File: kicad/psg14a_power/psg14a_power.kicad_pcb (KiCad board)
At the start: 2 copper layers, 9 parts, among them Q1 IRF9Z24N

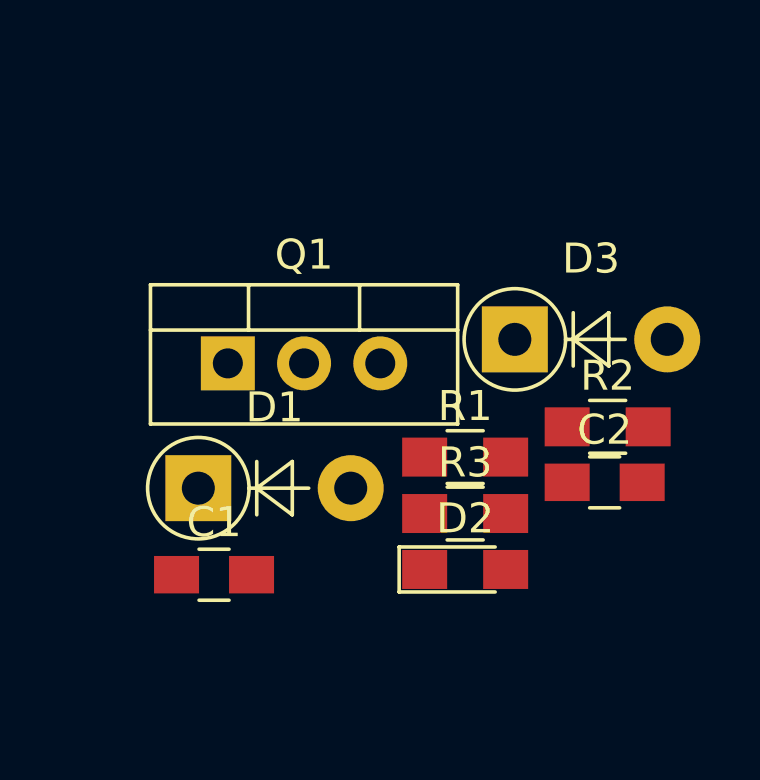
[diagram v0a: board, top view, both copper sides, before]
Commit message: [psg14a-power]Components placed
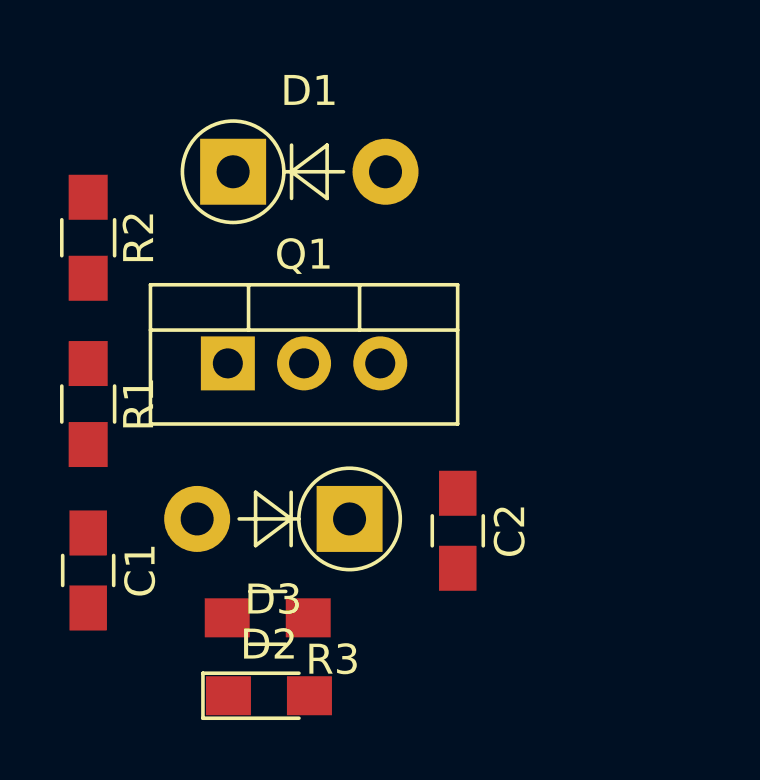
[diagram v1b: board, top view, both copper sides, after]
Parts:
- moved R2 18.4 mm to (44.2, 35.4), turned to 270 degrees
- moved R1 12.7 mm to (44.2, 40.9), turned to 270 degrees
- moved D1 10.6 mm to (49.1, 33.2)
- moved D3 8.13 mm to (52.9, 44.7), turned to 180 degrees
- moved D2 7.78 mm to (50.3, 50.6)
- moved R3 7.44 mm to (50.2, 48.0)
- moved C2 5.16 mm to (56.5, 45.1), turned to 270 degrees
- moved C1 4.20 mm to (44.2, 46.4), turned to 270 degrees
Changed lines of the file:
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@@
   )
   (module Capacitors_SMD:C_0805_HandSoldering (layer F.Cu)
-    (at 61.441721 43.509041)
+    (at 56.54548 45.12564 270)
     (descr "Capacitor SMD 0805, hand soldering")
     (tags "capacitor 0805")
     (attr smd)
-    (fp_text reference C2 (at 0 -1.75) (layer F.SilkS)
-      (effects (font (size 1 1) (thickness 0.15)))
-    )
-    (fp_text value "1uF 50V" (at 0 1.75) (layer F.Fab)
-      (effects (font (size 1 1) (thickness 0.15)))
-    )
-    (fp_text user %R (at 0 -1.75) (layer F.Fab)
+    (fp_text reference C2 (at 0 -1.75 270) (layer F.SilkS)
+      (effects (font (size 1 1) (thickness 0.15)))
+    )
+    (fp_text value "1uF 50V" (at 0 1.75 270) (layer F.Fab)
+      (effects (font (size 1 1) (thickness 0.15)))
+    )
+    (fp_text user %R (at 0 -1.75 270) (layer F.Fab)
       (effects (font (size 1 1) (thickness 0.15)))
     )
@@
     (fp_line (start 2.25 0.87) (end 2.25 -0.88) (layer F.CrtYd) (width 0.05))
     (fp_line (start 2.25 0.87) (end -2.25 0.87) (layer F.CrtYd) (width 0.05))
-    (pad 1 smd rect (at -1.25 0) (size 1.5 1.25) (layers F.Cu F.Paste F.Mask)
-      (net 1 /+24V))
-    (pad 2 smd rect (at 1.25 0) (size 1.5 1.25) (layers F.Cu F.Paste F.Mask)
+    (pad 1 smd rect (at -1.25 0 270) (size 1.5 1.25) (layers F.Cu F.Paste F.Mask)
+      (net 1 /+24V))
+    (pad 2 smd rect (at 1.25 0 270) (size 1.5 1.25) (layers F.Cu F.Paste F.Mask)
       (net 5 /gnd))
     (model Capacitors_SMD.3dshapes/C_0805.wrl
@@
   )
   (module Capacitors_SMD:C_0805_HandSoldering (layer F.Cu)
-    (at 48.421721 46.589041)
+    (at 44.22648 46.44644 270)
     (descr "Capacitor SMD 0805, hand soldering")
     (tags "capacitor 0805")
     (attr smd)
-    (fp_text reference C1 (at 0 -1.75) (layer F.SilkS)
-      (effects (font (size 1 1) (thickness 0.15)))
-    )
-    (fp_text value 10nF (at 0 1.75) (layer F.Fab)
+    (fp_text reference C1 (at 0 -1.75 270) (layer F.SilkS)
+      (effects (font (size 1 1) (thickness 0.15)))
+    )
+    (fp_text value 10nF (at 0 1.75 270) (layer F.Fab)
       (effects (font (size 1 1) (thickness 0.15)))
     )
@@
     (fp_line (start 1 0.62) (end -1 0.62) (layer F.Fab) (width 0.1))
     (fp_line (start -1 0.62) (end -1 -0.62) (layer F.Fab) (width 0.1))
-    (fp_text user %R (at 0 -1.75) (layer F.Fab)
-      (effects (font (size 1 1) (thickness 0.15)))
-    )
-    (pad 2 smd rect (at 1.25 0) (size 1.5 1.25) (layers F.Cu F.Paste F.Mask)
-      (net 3 "Net-(C1-Pad2)"))
-    (pad 1 smd rect (at -1.25 0) (size 1.5 1.25) (layers F.Cu F.Paste F.Mask)
+    (fp_text user %R (at 0 -1.75 270) (layer F.Fab)
+      (effects (font (size 1 1) (thickness 0.15)))
+    )
+    (pad 2 smd rect (at 1.25 0 270) (size 1.5 1.25) (layers F.Cu F.Paste F.Mask)
+      (net 3 "Net-(C1-Pad2)"))
+    (pad 1 smd rect (at -1.25 0 270) (size 1.5 1.25) (layers F.Cu F.Paste F.Mask)
       (net 1 /+24V))
     (model Capacitors_SMD.3dshapes/C_0805.wrl
@@
   )
   (module Diodes_THT:D_DO-41_SOD81_P5.08mm_Vertical_AnodeUp (layer F.Cu)
-    (at 58.447356 38.744041)
+    (at 52.93868 44.7294 180)
     (descr "D, DO-41_SOD81 series, Axial, Vertical, pin pitch=5.08mm, , length*diameter=5.2*2.7mm^2, , http://www.diodes.com/_files/packages/DO-41%20(Plastic).pdf")
     (tags "D DO-41_SOD81 series Axial Vertical pin pitch 5.08mm  length 5.2mm diameter 2.7mm")
-    (fp_text reference D3 (at 2.54 -2.690635) (layer F.SilkS)
-      (effects (font (size 1 1) (thickness 0.15)))
-    )
-    (fp_text value UF4007 (at 2.54 2.690635) (layer F.Fab)
-      (effects (font (size 1 1) (thickness 0.15)))
-    )
-    (fp_text user K (at -2.390635 0) (layer F.Fab)
-      (effects (font (size 1 1) (thickness 0.15)))
-    )
-    (fp_text user %R (at 2.54 0) (layer F.Fab)
+    (fp_text reference D3 (at 2.54 -2.690635 180) (layer F.SilkS)
+      (effects (font (size 1 1) (thickness 0.15)))
+    )
+    (fp_text value UF4007 (at 2.54 2.690635 180) (layer F.Fab)
+      (effects (font (size 1 1) (thickness 0.15)))
+    )
+    (fp_text user K (at -2.390635 0 180) (layer F.Fab)
+      (effects (font (size 1 1) (thickness 0.15)))
+    )
+    (fp_text user %R (at 2.54 0 180) (layer F.Fab)
       (effects (font (size 1 1) (thickness 0.15)))
     )
@@
     (fp_circle (center 0 0) (end 1.35 0) (layer F.Fab) (width 0.1))
     (fp_circle (center 0 0) (end 1.690635 0) (layer F.SilkS) (width 0.12))
-    (pad 1 thru_hole rect (at 0 0) (size 2.2 2.2) (drill 1.1) (layers *.Cu *.Mask)
+    (pad 1 thru_hole rect (at 0 0 180) (size 2.2 2.2) (drill 1.1) (layers *.Cu *.Mask)
       (net 2 "Net-(D2-Pad2)"))
-    (pad 2 thru_hole oval (at 5.08 0) (size 2.2 2.2) (drill 1.1) (layers *.Cu *.Mask)
+    (pad 2 thru_hole oval (at 5.08 0 180) (size 2.2 2.2) (drill 1.1) (layers *.Cu *.Mask)
       (net 7 /Relay_Ctl))
     (model ${KISYS3DMOD}/Diodes_THT.3dshapes/D_DO-41_SOD81_P5.08mm_Vertical_AnodeUp.wrl
@@
   )
   (module Diodes_THT:D_DO-41_SOD81_P5.08mm_Vertical_AnodeUp (layer F.Cu)
-    (at 47.897356 43.704041)
+    (at 49.05756 33.15716)
     (descr "D, DO-41_SOD81 series, Axial, Vertical, pin pitch=5.08mm, , length*diameter=5.2*2.7mm^2, , http://www.diodes.com/_files/packages/DO-41%20(Plastic).pdf")
     (tags "D DO-41_SOD81 series Axial Vertical pin pitch 5.08mm  length 5.2mm diameter 2.7mm")
@@
       (effects (font (size 1 1) (thickness 0.15)))
     )
-    (fp_text value BZX85_C12 (at 2.54 2.690635) (layer F.Fab)
+    (fp_text value BZX85_C12 (at 2.54 2.690635 90) (layer F.Fab)
       (effects (font (size 1 1) (thickness 0.15)))
     )
@@
   )
   (module LEDs:LED_0805_HandSoldering (layer F.Cu)
-    (at 56.791721 46.414041)
+    (at 50.25136 50.6222)
     (descr "Resistor SMD 0805, hand soldering")
     (tags "resistor 0805")
@@
   )
   (module Resistors_SMD:R_0805_HandSoldering (layer F.Cu)
-    (at 56.791721 44.549041)
-    (descr "Resistor SMD 0805, hand soldering")
-    (tags "resistor 0805")
-    (attr smd)
-    (fp_text reference R3 (at 0 -1.7) (layer F.SilkS)
-      (effects (font (size 1 1) (thickness 0.15)))
-    )
-    (fp_text value 5k1 (at 0 1.75) (layer F.Fab)
+    (at 50.21072 48.02632)
+    (descr "Resistor SMD 0805, hand soldering")
+    (tags "resistor 0805")
+    (attr smd)
+    (fp_text reference R3 (at 2.166759 1.399559) (layer F.SilkS)
+      (effects (font (size 1 1) (thickness 0.15)))
+    )
+    (fp_text value 5k1 (at -0.61468 2.42316) (layer F.Fab)
       (effects (font (size 1 1) (thickness 0.15)))
     )
@@
   )
   (module Resistors_SMD:R_0805_HandSoldering (layer F.Cu)
-    (at 61.541721 41.659041)
-    (descr "Resistor SMD 0805, hand soldering")
-    (tags "resistor 0805")
-    (attr smd)
-    (fp_text reference R2 (at 0 -1.7) (layer F.SilkS)
-      (effects (font (size 1 1) (thickness 0.15)))
-    )
-    (fp_text value 10K (at 0 1.75) (layer F.Fab)
-      (effects (font (size 1 1) (thickness 0.15)))
-    )
-    (fp_text user %R (at 0 0) (layer F.Fab)
+    (at 44.22648 35.3568 270)
+    (descr "Resistor SMD 0805, hand soldering")
+    (tags "resistor 0805")
+    (attr smd)
+    (fp_text reference R2 (at 0 -1.7 270) (layer F.SilkS)
+      (effects (font (size 1 1) (thickness 0.15)))
+    )
+    (fp_text value 10K (at 0 1.75 270) (layer F.Fab)
+      (effects (font (size 1 1) (thickness 0.15)))
+    )
+    (fp_text user %R (at 0 0 270) (layer F.Fab)
       (effects (font (size 0.5 0.5) (thickness 0.075)))
     )
@@
     (fp_line (start 2.35 0.9) (end 2.35 -0.9) (layer F.CrtYd) (width 0.05))
     (fp_line (start 2.35 0.9) (end -2.35 0.9) (layer F.CrtYd) (width 0.05))
-    (pad 1 smd rect (at -1.35 0) (size 1.5 1.3) (layers F.Cu F.Paste F.Mask)
-      (net 1 /+24V))
-    (pad 2 smd rect (at 1.35 0) (size 1.5 1.3) (layers F.Cu F.Paste F.Mask)
+    (pad 1 smd rect (at -1.35 0 270) (size 1.5 1.3) (layers F.Cu F.Paste F.Mask)
+      (net 1 /+24V))
+    (pad 2 smd rect (at 1.35 0 270) (size 1.5 1.3) (layers F.Cu F.Paste F.Mask)
       (net 3 "Net-(C1-Pad2)"))
     (model ${KISYS3DMOD}/Resistors_SMD.3dshapes/R_0805.wrl
@@
   )
   (module Resistors_SMD:R_0805_HandSoldering (layer F.Cu)
-    (at 56.791721 42.669041)
-    (descr "Resistor SMD 0805, hand soldering")
-    (tags "resistor 0805")
-    (attr smd)
-    (fp_text reference R1 (at 0 -1.7) (layer F.SilkS)
-      (effects (font (size 1 1) (thickness 0.15)))
-    )
-    (fp_text value 10K (at 0 1.75) (layer F.Fab)
+    (at 44.22648 40.89908 270)
+    (descr "Resistor SMD 0805, hand soldering")
+    (tags "resistor 0805")
+    (attr smd)
+    (fp_text reference R1 (at 0 -1.7 270) (layer F.SilkS)
+      (effects (font (size 1 1) (thickness 0.15)))
+    )
+    (fp_text value 10K (at 0 1.75 270) (layer F.Fab)
       (effects (font (size 1 1) (thickness 0.15)))
     )
@@
     (fp_line (start 1 0.62) (end -1 0.62) (layer F.Fab) (width 0.1))
     (fp_line (start -1 0.62) (end -1 -0.62) (layer F.Fab) (width 0.1))
-    (fp_text user %R (at 0 0) (layer F.Fab)
+    (fp_text user %R (at 0 0 270) (layer F.Fab)
       (effects (font (size 0.5 0.5) (thickness 0.075)))
     )
-    (pad 2 smd rect (at 1.35 0) (size 1.5 1.3) (layers F.Cu F.Paste F.Mask)
+    (pad 2 smd rect (at 1.35 0 270) (size 1.5 1.3) (layers F.Cu F.Paste F.Mask)
       (net 4 /In))
-    (pad 1 smd rect (at -1.35 0) (size 1.5 1.3) (layers F.Cu F.Paste F.Mask)
+    (pad 1 smd rect (at -1.35 0 270) (size 1.5 1.3) (layers F.Cu F.Paste F.Mask)
       (net 3 "Net-(C1-Pad2)"))
     (model ${KISYS3DMOD}/Resistors_SMD.3dshapes/R_0805.wrl

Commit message: [psg14a] looking how to copy blocks
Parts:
- added C1: 10nF, Capacitors_SMD:C_0805_HandSoldering, F.Cu at (112.2, 46.4)
- added C1: 10nF, Capacitors_SMD:C_0805_HandSoldering, F.Cu at (95.2, 46.4)
- added C1: 10nF, Capacitors_SMD:C_0805_HandSoldering, F.Cu at (78.2, 46.4)
- added C1: 10nF, Capacitors_SMD:C_0805_HandSoldering, F.Cu at (61.2, 46.4)
- added C10: 1uF 50V, Capacitors_SMD:C_0805_HandSoldering, F.Cu at (133.4, 38.9)
- added C2: 1uF 50V, Capacitors_SMD:C_0805_HandSoldering, F.Cu at (124.5, 45.1)
- added C2: 1uF 50V, Capacitors_SMD:C_0805_HandSoldering, F.Cu at (107.5, 45.1)
- added C2: 1uF 50V, Capacitors_SMD:C_0805_HandSoldering, F.Cu at (90.5, 45.1)
- added C2: 1uF 50V, Capacitors_SMD:C_0805_HandSoldering, F.Cu at (73.5, 45.1)
- added C3: 10nF, Capacitors_SMD:C_0805_HandSoldering, F.Cu at (133.4, 42.5)
- added C4: 10nF, Capacitors_SMD:C_0805_HandSoldering, F.Cu at (133.4, 40.7)
- added C5: 1uF 50V, Capacitors_SMD:C_0805_HandSoldering, F.Cu at (128.7, 44.4)
- added C6: 1uF 50V, Capacitors_SMD:C_0805_HandSoldering, F.Cu at (123.9, 47.5)
- added C7: 10nF, Capacitors_SMD:C_0805_HandSoldering, F.Cu at (123.9, 45.7)
- added C8: 1uF 50V, Capacitors_SMD:C_0805_HandSoldering, F.Cu at (121.6, 49.4)
- added C9: 10nF, Capacitors_SMD:C_0805_HandSoldering, F.Cu at (128.7, 42.6)
- added D1: BZX85_C12, Diodes_THT:D_DO-41_SOD81_P5.08mm_Vertical_AnodeUp, F.Cu at (117.1, 33.2)
- added D1: BZX85_C12, Diodes_THT:D_DO-41_SOD81_P5.08mm_Vertical_AnodeUp, F.Cu at (100.1, 33.2)
- added D1: BZX85_C12, Diodes_THT:D_DO-41_SOD81_P5.08mm_Vertical_AnodeUp, F.Cu at (83.1, 33.2)
- added D1: BZX85_C12, Diodes_THT:D_DO-41_SOD81_P5.08mm_Vertical_AnodeUp, F.Cu at (66.1, 33.2)
- added D10: BZX85_C12, Diodes_THT:D_DO-41_SOD81_P5.08mm_Vertical_AnodeUp, F.Cu at (118.6, 37.2)
- added D11: green, LEDs:LED_0805_HandSoldering, F.Cu at (119.3, 47.6)
- added D12: UF4007, Diodes_THT:D_DO-41_SOD81_P5.08mm_Vertical_AnodeUp, F.Cu at (110.4, 45.1)
- added D13: BZX85_C12, Diodes_THT:D_DO-41_SOD81_P5.08mm_Vertical_AnodeUp, F.Cu at (108.1, 49.1)
- added D14: green, LEDs:LED_0805_HandSoldering, F.Cu at (119.3, 45.7)
- added D15: UF4007, Diodes_THT:D_DO-41_SOD81_P5.08mm_Vertical_AnodeUp, F.Cu at (129.2, 32.2)
- added D2: green, LEDs:LED_0805_HandSoldering, F.Cu at (118.3, 50.6)
- added D2: green, LEDs:LED_0805_HandSoldering, F.Cu at (101.3, 50.6)
- added D2: green, LEDs:LED_0805_HandSoldering, F.Cu at (84.3, 50.6)
- added D2: green, LEDs:LED_0805_HandSoldering, F.Cu at (67.3, 50.6)
- added D3: UF4007, Diodes_THT:D_DO-41_SOD81_P5.08mm_Vertical_AnodeUp, F.Cu at (120.9, 44.7)
- added D3: UF4007, Diodes_THT:D_DO-41_SOD81_P5.08mm_Vertical_AnodeUp, F.Cu at (103.9, 44.7)
- added D3: UF4007, Diodes_THT:D_DO-41_SOD81_P5.08mm_Vertical_AnodeUp, F.Cu at (86.9, 44.7)
- added D3: UF4007, Diodes_THT:D_DO-41_SOD81_P5.08mm_Vertical_AnodeUp, F.Cu at (69.9, 44.7)
- added D4: BZX85_C12, Diodes_THT:D_DO-41_SOD81_P5.08mm_Vertical_AnodeUp, F.Cu at (110.4, 37.2)
- added D5: BZX85_C12, Diodes_THT:D_DO-41_SOD81_P5.08mm_Vertical_AnodeUp, F.Cu at (99.8, 47.1)
- added D6: green, LEDs:LED_0805_HandSoldering, F.Cu at (128.8, 40.8)
- added D7: green, LEDs:LED_0805_HandSoldering, F.Cu at (132.3, 37.0)
- added D8: UF4007, Diodes_THT:D_DO-41_SOD81_P5.08mm_Vertical_AnodeUp, F.Cu at (120.9, 32.2)
- added D9: UF4007, Diodes_THT:D_DO-41_SOD81_P5.08mm_Vertical_AnodeUp, F.Cu at (110.4, 41.2)
- added Q1: IRF9Z24N, TO_SOT_Packages_THT:TO-220-3_Vertical, F.Cu at (116.9, 39.5)
- added Q1: IRF9Z24N, TO_SOT_Packages_THT:TO-220-3_Vertical, F.Cu at (99.9, 39.5)
- added Q1: IRF9Z24N, TO_SOT_Packages_THT:TO-220-3_Vertical, F.Cu at (82.9, 39.5)
- added Q1: IRF9Z24N, TO_SOT_Packages_THT:TO-220-3_Vertical, F.Cu at (65.9, 39.5)
- added Q2: IRF9Z24N, TO_SOT_Packages_THT:TO-220-3_Vertical, F.Cu at (100.8, 43.0)
- added Q3: IRF9Z24N, TO_SOT_Packages_THT:TO-220-3_Vertical, F.Cu at (100.8, 38.0)
- added Q4: IRF9Z24N, TO_SOT_Packages_THT:TO-220-3_Vertical, F.Cu at (100.8, 33.0)
- added Q5: IRF9Z24N, TO_SOT_Packages_THT:TO-220-3_Vertical, F.Cu at (111.4, 33.0)
- added R1: 10K, Resistors_SMD:R_0805_HandSoldering, F.Cu at (112.2, 40.9)
- added R1: 10K, Resistors_SMD:R_0805_HandSoldering, F.Cu at (95.2, 40.9)
- added R1: 10K, Resistors_SMD:R_0805_HandSoldering, F.Cu at (78.2, 40.9)
- added R1: 10K, Resistors_SMD:R_0805_HandSoldering, F.Cu at (61.2, 40.9)
- added R10: 10K, Resistors_SMD:R_0805_HandSoldering, F.Cu at (119.3, 43.9)
- added R11: 10K, Resistors_SMD:R_0805_HandSoldering, F.Cu at (128.8, 38.9)
- added R12: 5k1, Resistors_SMD:R_0805_HandSoldering, F.Cu at (119.3, 42.0)
- added R13: 10K, Resistors_SMD:R_0805_HandSoldering, F.Cu at (127.5, 35.2)
- added R14: 10K, Resistors_SMD:R_0805_HandSoldering, F.Cu at (119.3, 40.1)
- added R15: 5k1, Resistors_SMD:R_0805_HandSoldering, F.Cu at (117.0, 49.5)
- added R2: 10K, Resistors_SMD:R_0805_HandSoldering, F.Cu at (112.2, 35.4)
- added R2: 10K, Resistors_SMD:R_0805_HandSoldering, F.Cu at (95.2, 35.4)
- added R2: 10K, Resistors_SMD:R_0805_HandSoldering, F.Cu at (78.2, 35.4)
- added R2: 10K, Resistors_SMD:R_0805_HandSoldering, F.Cu at (61.2, 35.4)
- added R3: 5k1, Resistors_SMD:R_0805_HandSoldering, F.Cu at (118.2, 48.0)
- added R3: 5k1, Resistors_SMD:R_0805_HandSoldering, F.Cu at (101.2, 48.0)
- added R3: 5k1, Resistors_SMD:R_0805_HandSoldering, F.Cu at (84.2, 48.0)
- added R3: 5k1, Resistors_SMD:R_0805_HandSoldering, F.Cu at (67.2, 48.0)
- added R4: 10K, Resistors_SMD:R_0805_HandSoldering, F.Cu at (124.0, 43.9)
- added R5: 10K, Resistors_SMD:R_0805_HandSoldering, F.Cu at (124.0, 42.0)
- added R6: 10K, Resistors_SMD:R_0805_HandSoldering, F.Cu at (100.4, 50.0)
- added R7: 5k1, Resistors_SMD:R_0805_HandSoldering, F.Cu at (124.0, 40.1)
- added R8: 10K, Resistors_SMD:R_0805_HandSoldering, F.Cu at (127.5, 37.0)
- added R9: 5k1, Resistors_SMD:R_0805_HandSoldering, F.Cu at (132.3, 35.2)
- turned R2 to 90 degrees
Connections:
- D2 pad 2: Net-(D2-Pad2) -> /Relay_Ctl
- D3 pad 1: Net-(D2-Pad2) -> /Relay_Ctl
- D3 pad 2: /Relay_Ctl -> Net-(D3-Pad2)
- Q1 pad 2: Net-(D2-Pad2) -> /Relay_Ctl
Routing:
- net /+24V: track 0.00 -> 252.7 mm
- net Net-(C1-Pad2): track 0.00 -> 145.6 mm
- net /Relay_Ctl: track 0.00 -> 72.0 mm, vias 0 -> 5
- net /gnd: track 0.00 -> 60.2 mm
- net Net-(D2-Pad1): track 0.00 -> 13.1 mm
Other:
- net class Default: clearance 0.2 -> 0.25; trace_width 0.25 -> 0.4; via_dia 0.8 -> 1; via_drill 0.4 -> 0.5
- rule trace_clearance: 0.2 -> 0.25
